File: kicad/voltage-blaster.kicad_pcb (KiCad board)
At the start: 2 copper layers, 95.2 x 24.1 mm, 6 parts, among them J1 Bus_ISA_8bit, U1 LM7905

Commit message: Add some markings on the back side.
This is actually not necessary, but having this markings there will
enforce JLCPCB to print their serial number on the back side as well
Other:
- board text added: "PC back <-----"

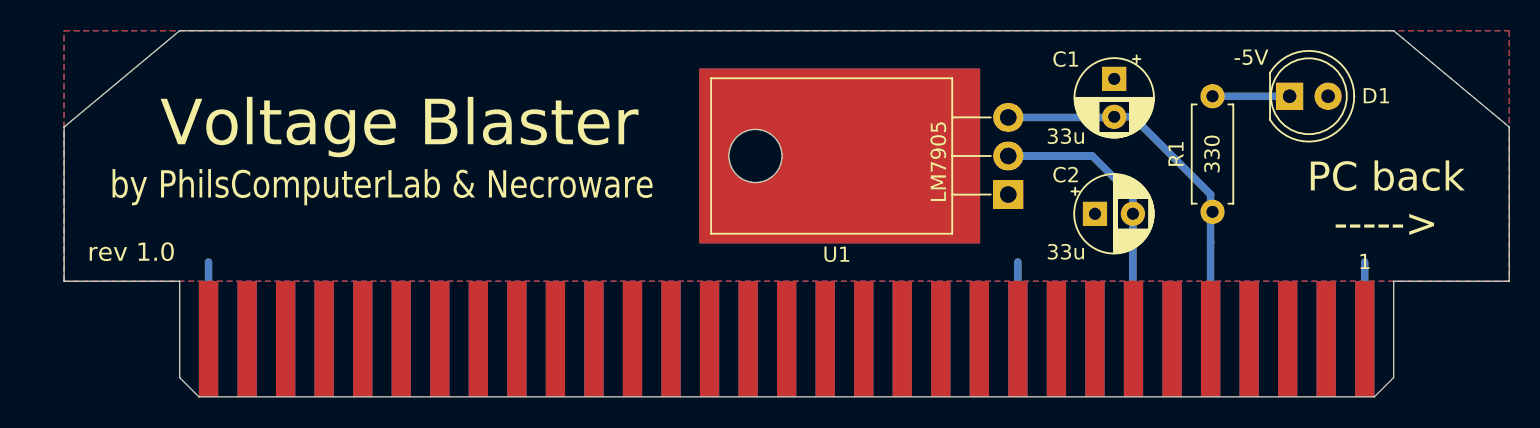
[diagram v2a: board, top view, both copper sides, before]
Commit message: Improved PCB layout
- removed solder mask on LM7905 cooling area
- increased cooling area on the back side
- added micro vias for better thermal transport
- removed unused socket pins
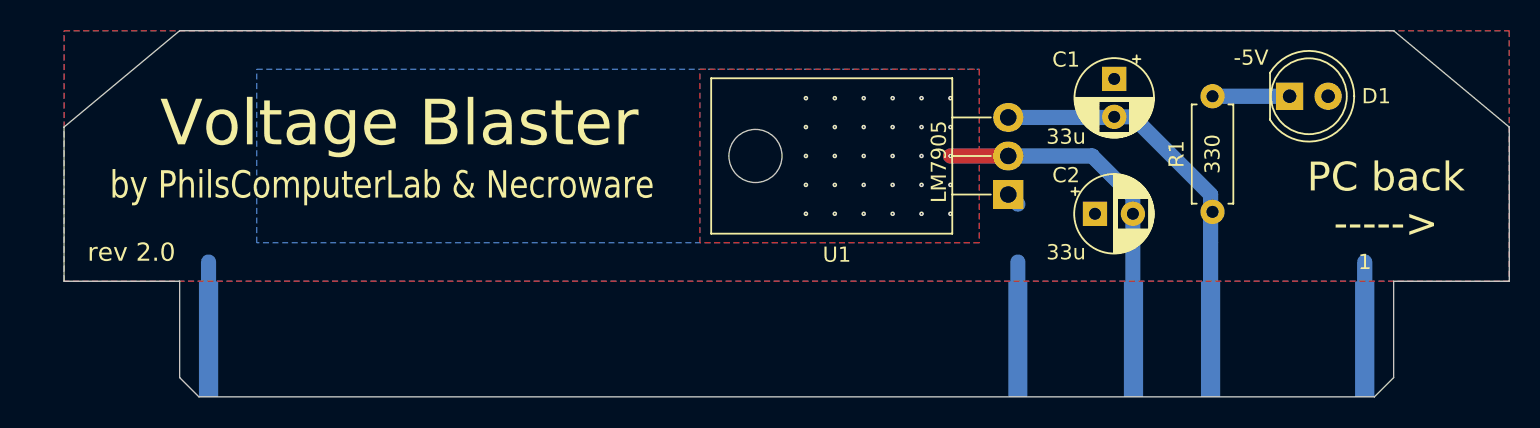
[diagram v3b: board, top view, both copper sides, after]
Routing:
- net Net-(C2-Pad2): track 18.7 -> 26.3 mm, vias 0 -> 30
- added copper zone on B.Cu, net Net-(C2-Pad2)
- added copper zone on F.Cu, net Net-(C2-Pad2)
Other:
- net class Default: clearance 0.4 -> 0.5; trace_width 0.5 -> 1
- rule trace_clearance: 0.4 -> 0.5
- board text added: "rev 2.0"
- board text removed: "rev 1.0"
